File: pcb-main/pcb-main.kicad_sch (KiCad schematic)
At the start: 37 parts, among them J1 AVR-ISP-6, J2 Conn_02x06_Counter_Clockwise, M1 Stepper_Motor, SW1 SW_MEC_5E, SW2 SW_MEC_5E, U1 ATmega328P-AU, U2 HT1621B-LQFP-A, U3 VIM878, U4 PCF8563T, Y1 Crystal_GND24, Y2 32kHz

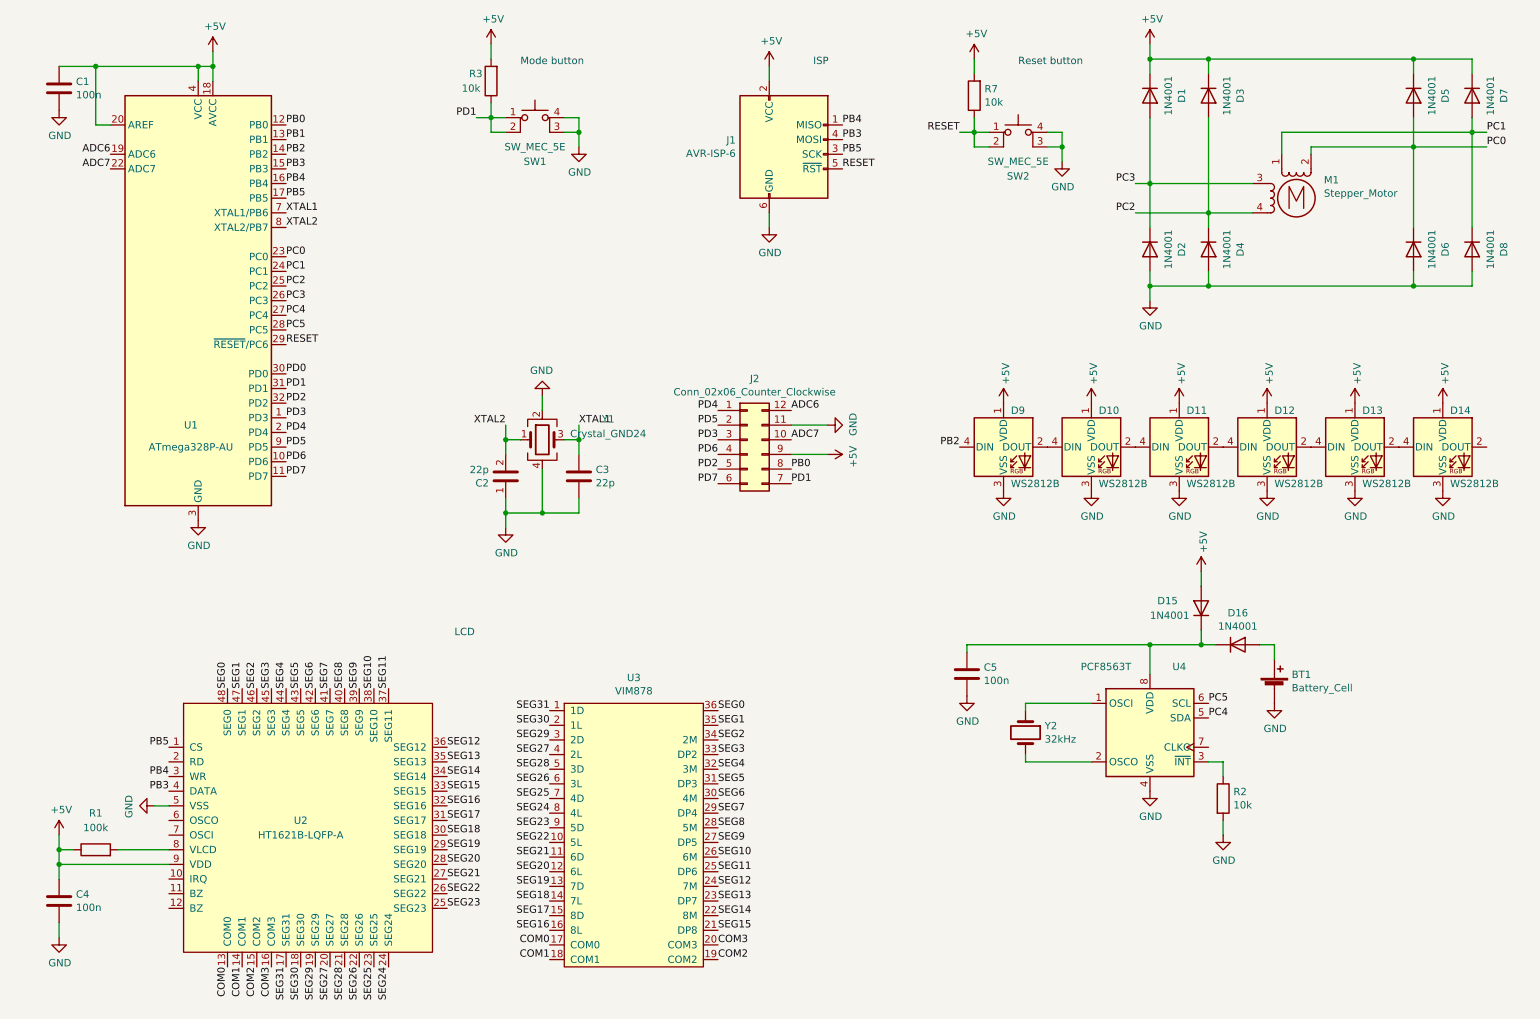
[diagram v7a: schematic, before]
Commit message: resolves #48: neopixel caps
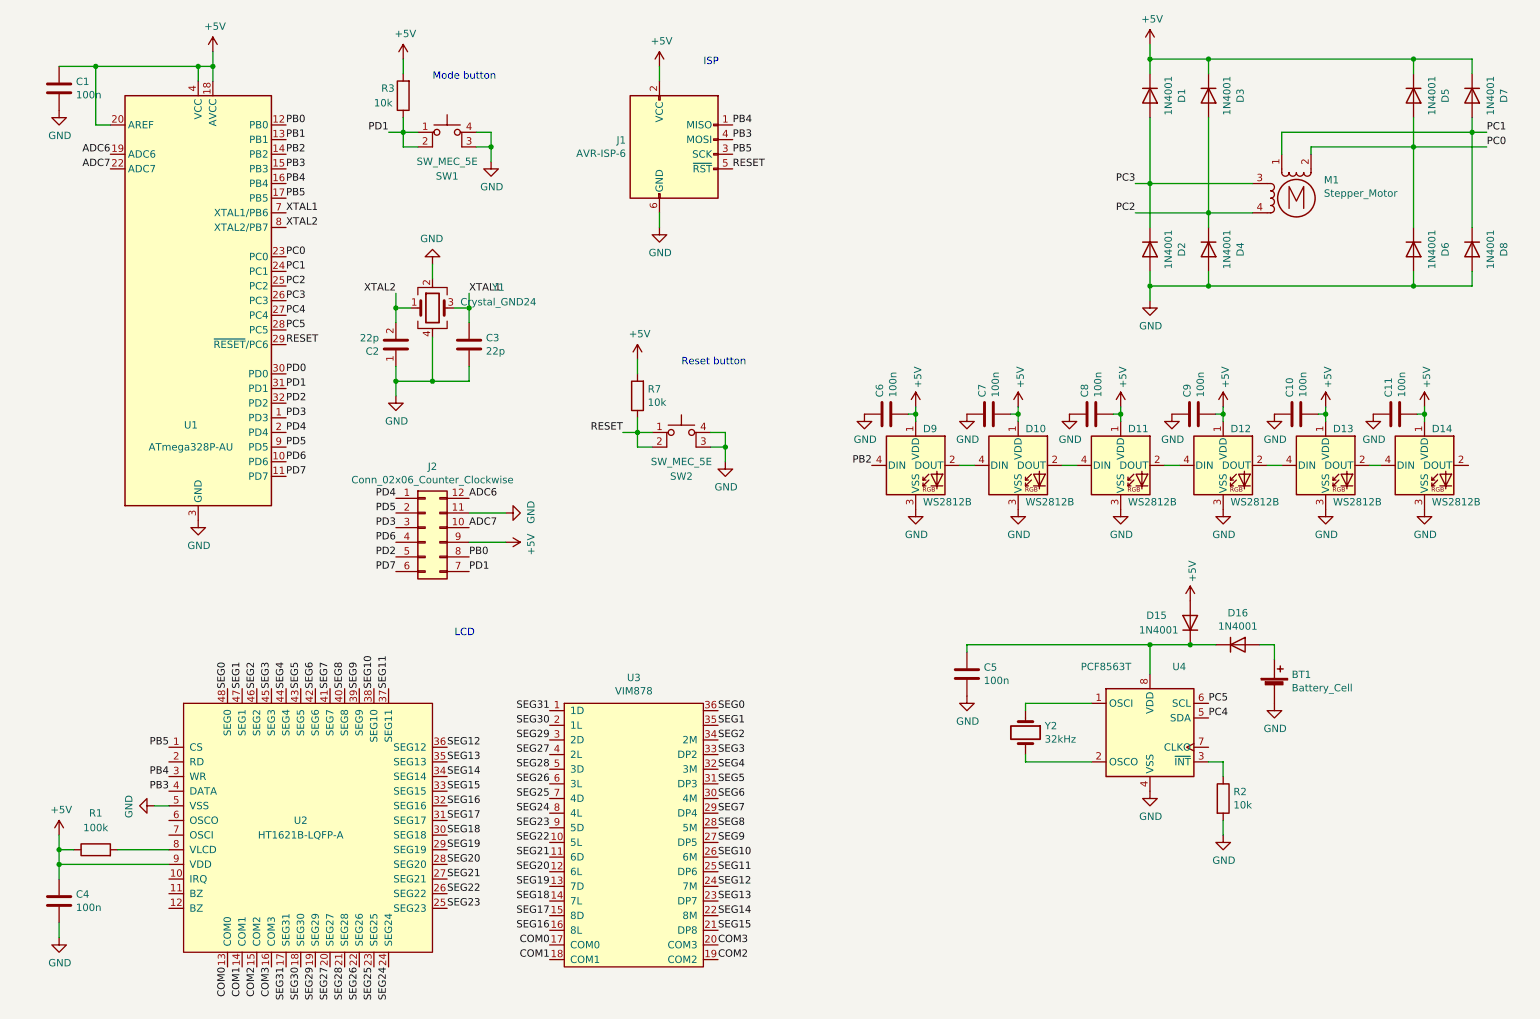
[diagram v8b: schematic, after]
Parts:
- added C10, C11, C6, C7, C8, C9: 100n, Capacitor_SMD:C_0805_2012Metric, symbol Device:C
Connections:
- net +5V: now also C10.2, C11.2, C6.2, C7.2, C8.2, C9.2
- net GND: now also C10.1, C11.1, C6.1, C7.1, C8.1, C9.1
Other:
- moved on the sheet: C2, C3, D10, D11, D12, D13, D14, D15, D9, J1, J2, R3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
